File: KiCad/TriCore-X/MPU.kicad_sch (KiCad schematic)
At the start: 3 parts, among them U1 CH334P, U7 T113-S3_C5197687

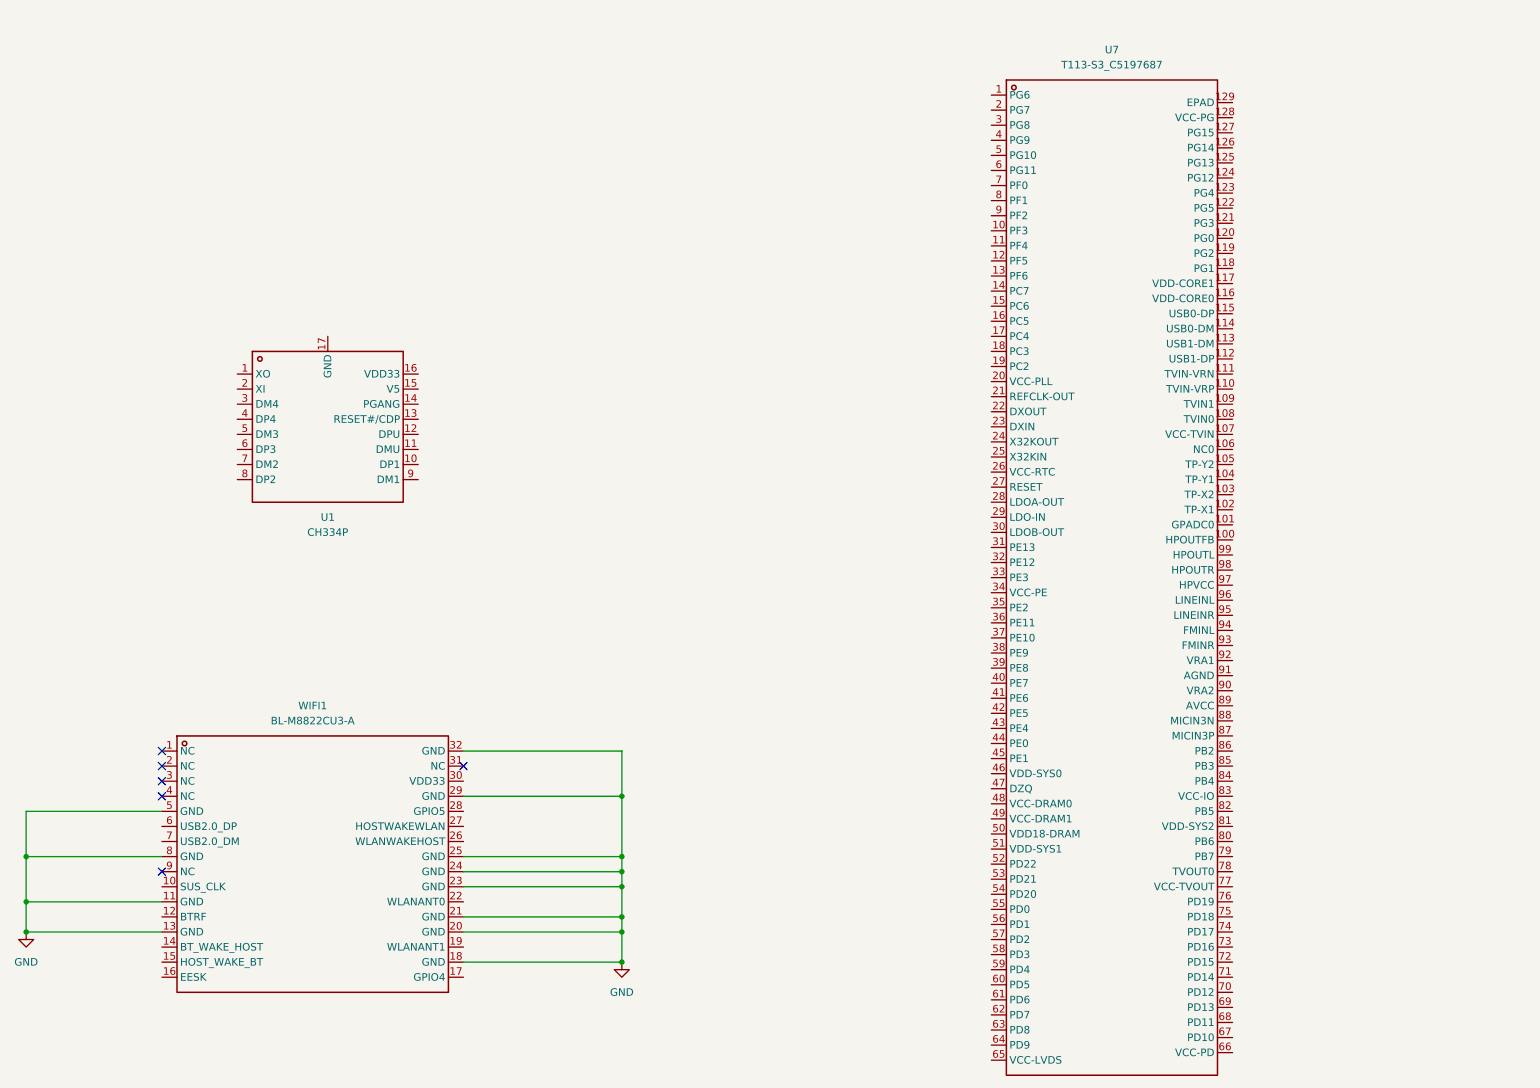
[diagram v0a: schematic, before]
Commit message: refactor: update schematic components, remove unused files, and add new LED and CH334P symbols
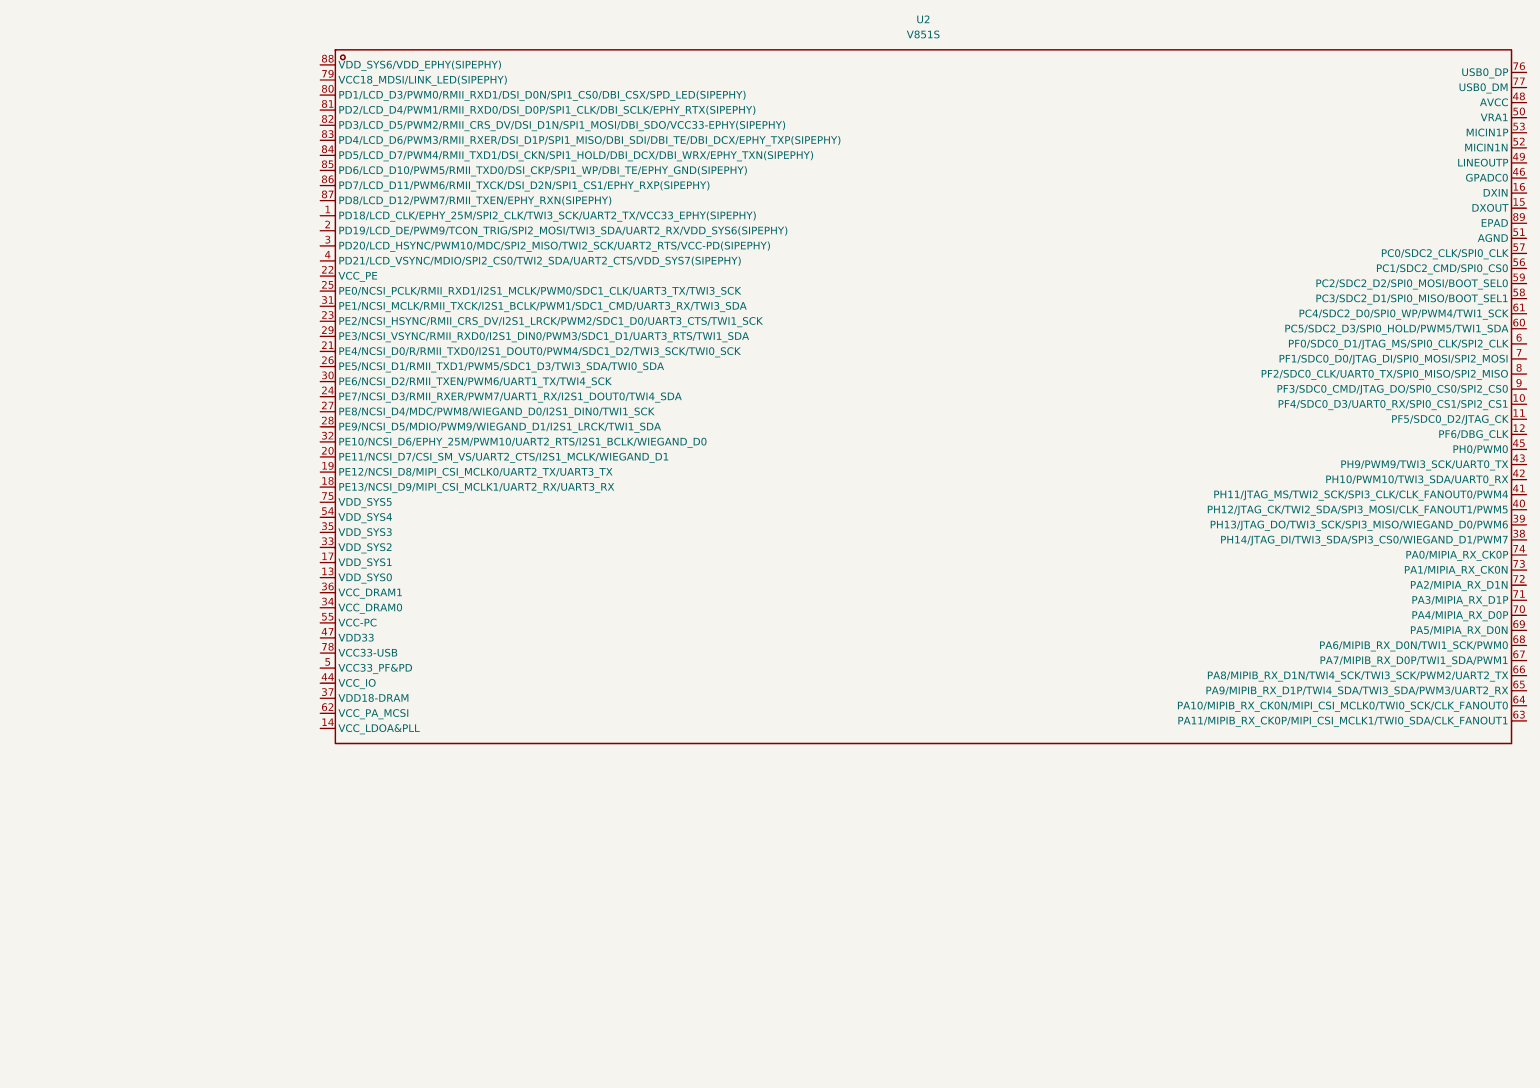
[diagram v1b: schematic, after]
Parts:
- removed U1: CH334P, CH334P:QFN-16_L3.0-W3.0-P0.50-BL-EP1.7, symbol CH334P:CH334P
- removed U7: T113-S3_C5197687, T113-S3:LQFP-128_L14.0-W14.0-P0.40-LS16.0-BL-EP5.6, symbol T113-S3:T113-S3_C5197687
- removed WIFI1: BL-M8822CU3-A, BL-M8822CU3-A:WIRELM-SMD_BL-M8822CU3-A, symbol BL-M8822CU3-A:BL-M8822CU3-A
- added U2: V851S, V851s:QFN-88_L9.0-W9.0-P0.35-TL-EP6.5, symbol V851s:V851S
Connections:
- no-connect marks 6 -> 0
